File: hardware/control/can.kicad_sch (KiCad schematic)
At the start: 9 parts, among them U301 MCP2561

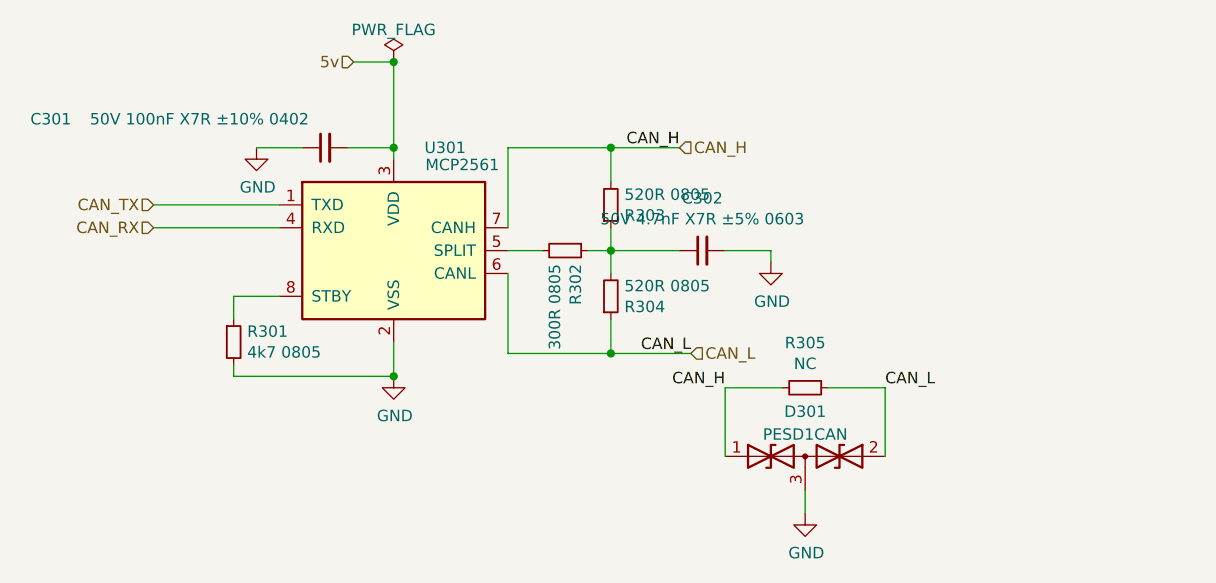
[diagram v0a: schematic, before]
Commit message: Organize schematics per domain
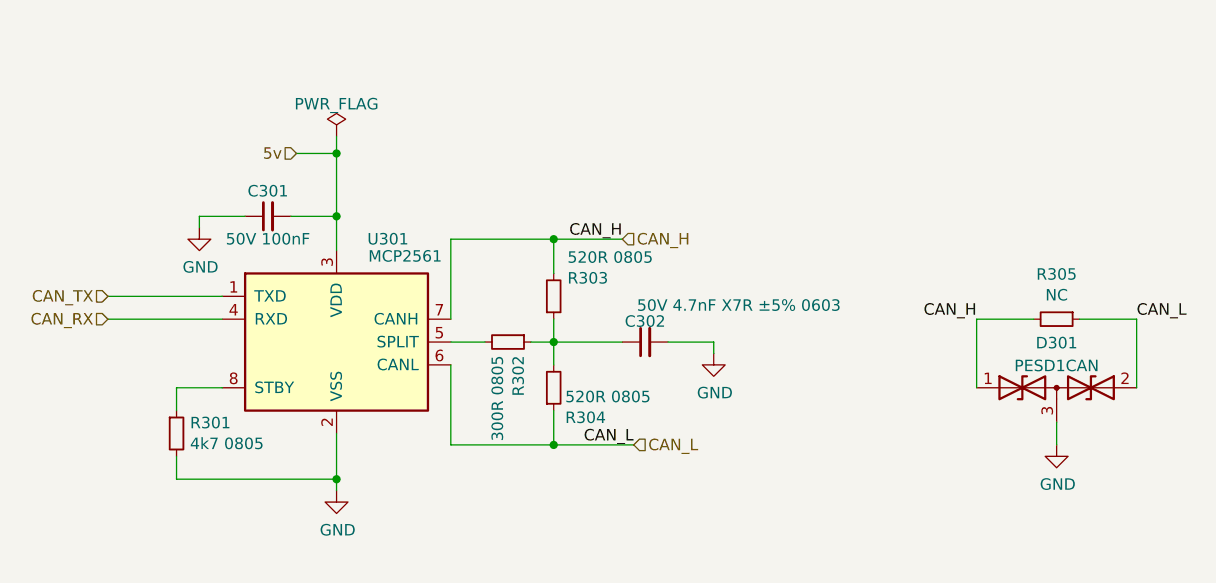
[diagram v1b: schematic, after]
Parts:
- C301: value 50V 100nF X7R ±10% 0402 -> 50V 100nF
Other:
- company: (none) -> Zenite Solar
- title: (none) -> CAN
- moved on the sheet: C301, C302, D301, R301, R302, R303, R304, R305, U301
